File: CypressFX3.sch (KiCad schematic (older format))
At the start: 58 parts, among them CON2 AVR-JTAG-10, IC3 CyUSB30xx-BZX, J6 GSB3211311WEU, Q1 IRLML2502, Y1 19.2MHz

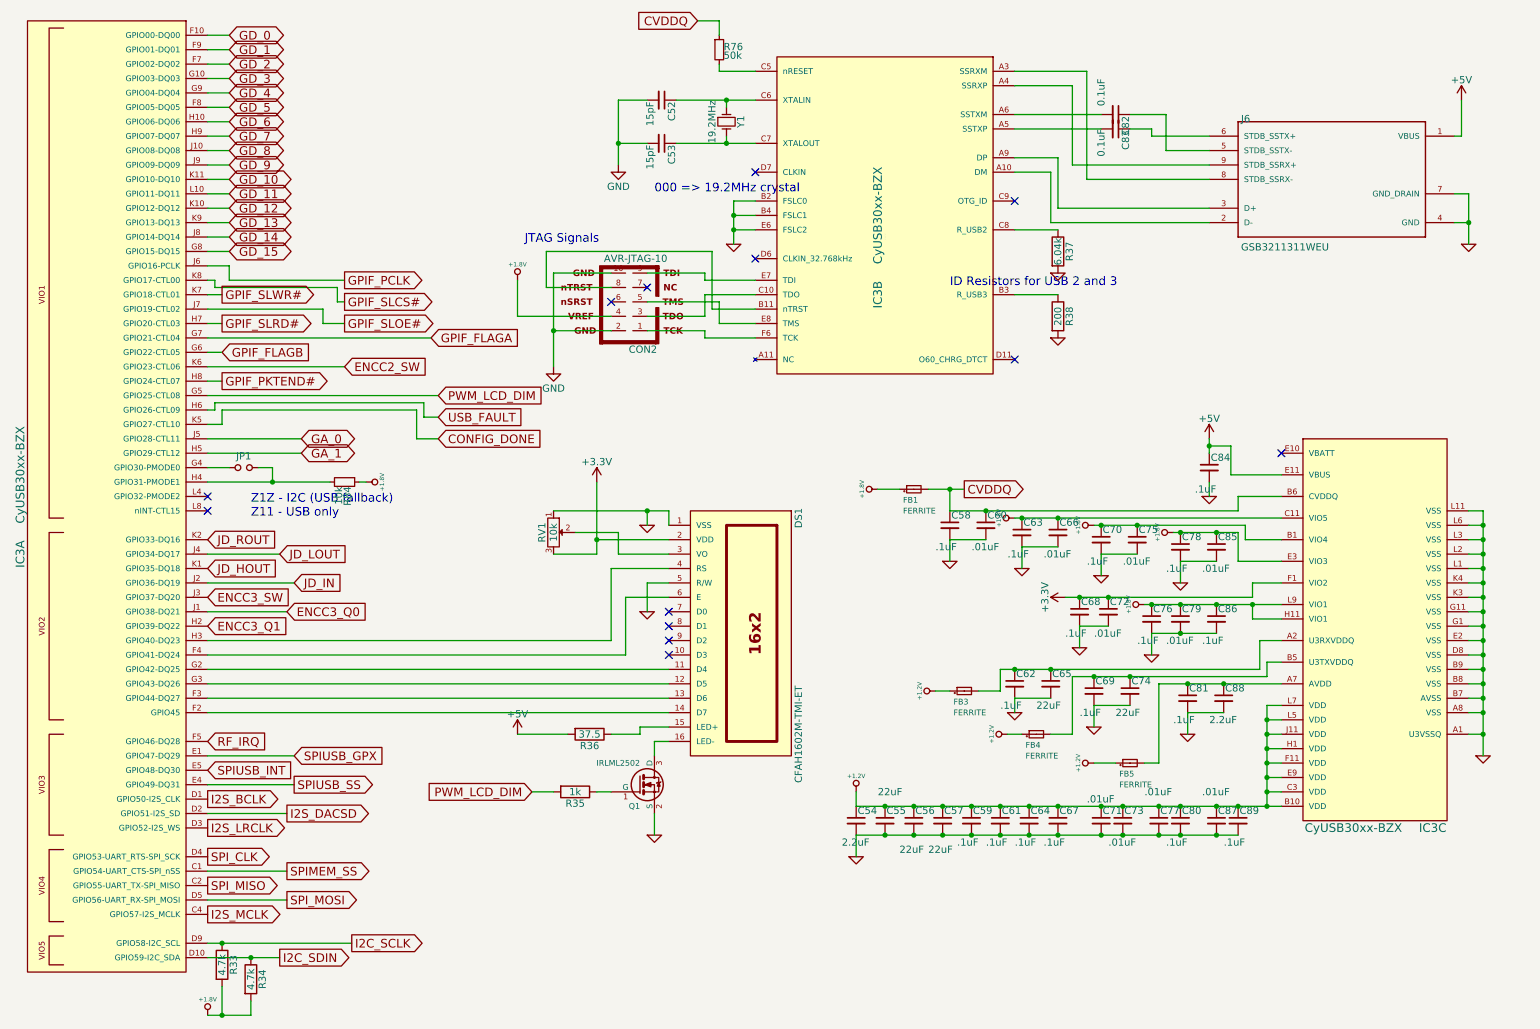
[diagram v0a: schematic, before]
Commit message: fixed all schematic/footprint errors
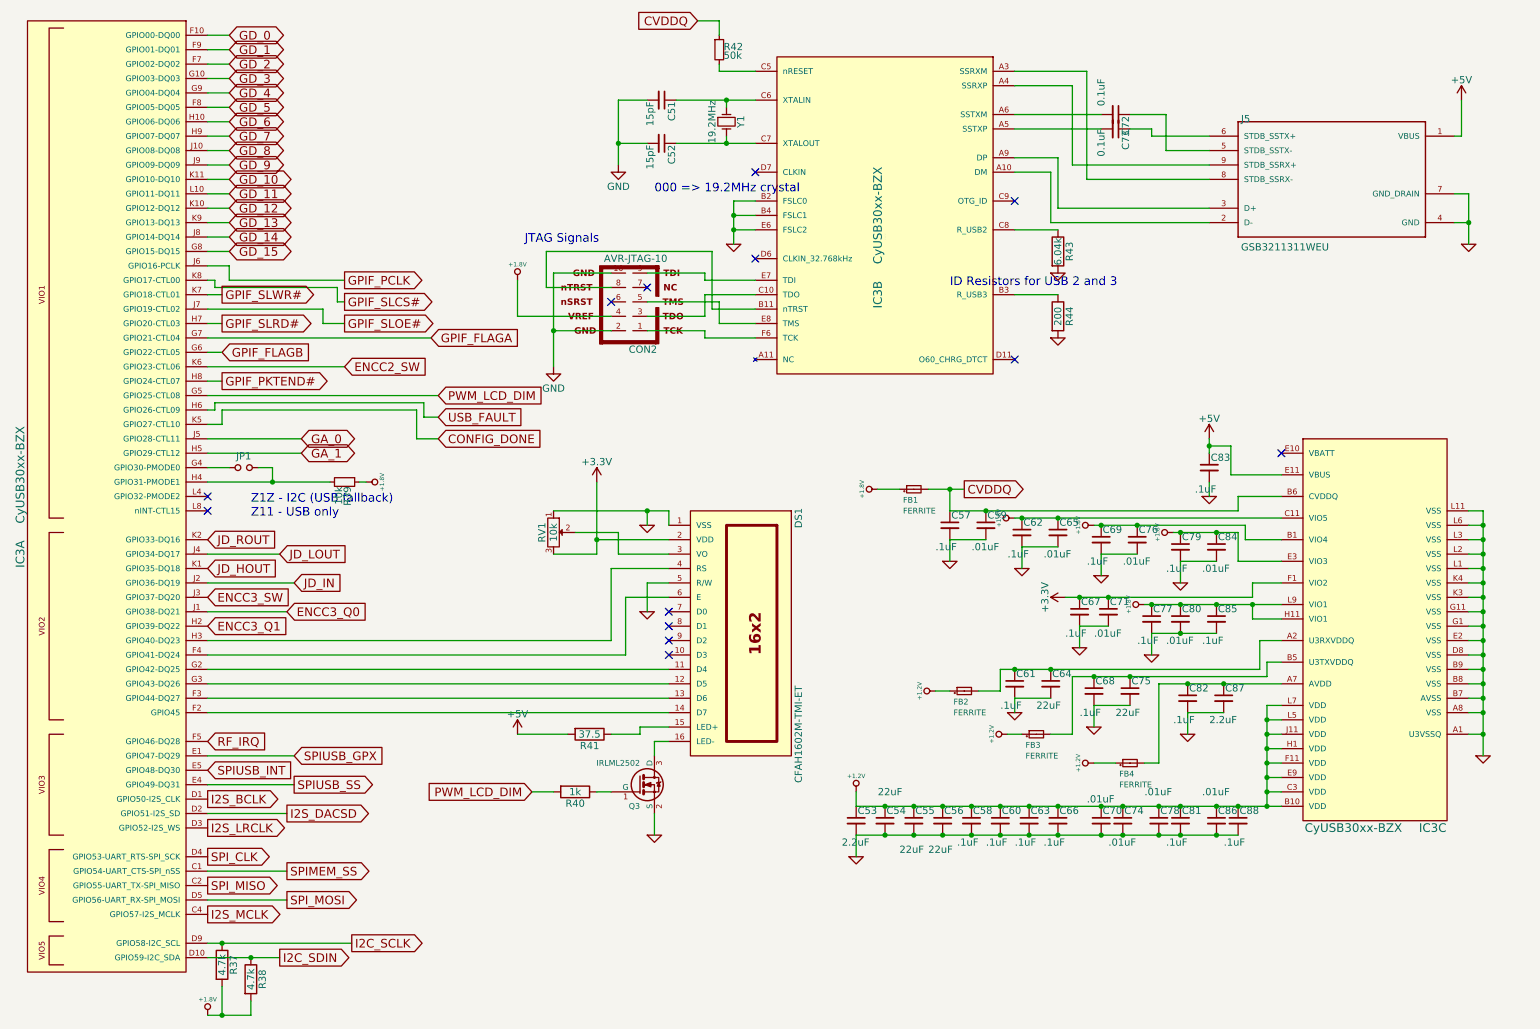
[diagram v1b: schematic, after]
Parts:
- renumbered C52 to C51, C53 to C52, C54 to C53, C55 to C54, C56 to C55, C57 to C56, C58 to C57, C59 to C58, C60 to C59, C61 to C60, C62 to C61, C63 to C62, C64 to C63, C65 to C64, C66 to C65, C67 to C66, C68 to C67, C69 to C68, C70 to C69, C71 to C70, C72 to C71, C82 to C72, C83 to C73, C73 to C74, C74 to C75, C75 to C76, C76 to C77, C77 to C78, C78 to C79, C79 to C80, C80 to C81, C81 to C82, C84 to C83, C85 to C84, C86 to C85, C87 to C86, C88 to C87, C89 to C88, FB3 to FB2, FB4 to FB3, FB5 to FB4, J6 to J5, Q1 to Q3, R33 to R37, R34 to R38, R84 to R39, R35 to R40, R36 to R41, R76 to R42, R37 to R43, R38 to R44

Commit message: started PCBnew trivial connections and BGA interface, shuffled some net connections, etc.
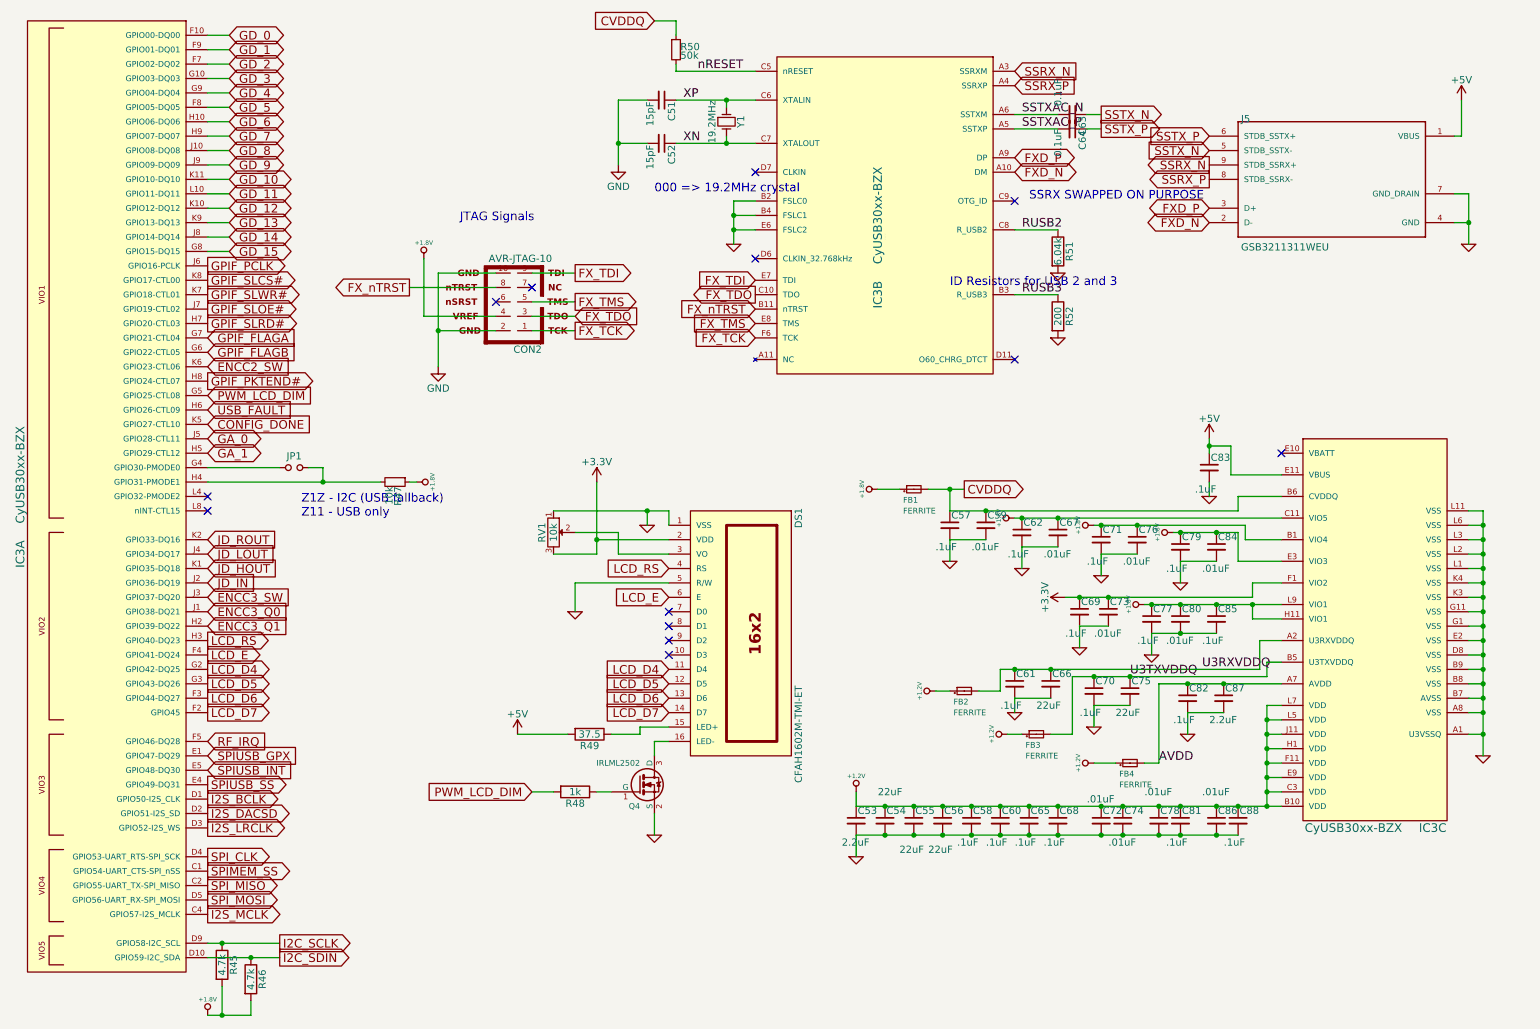
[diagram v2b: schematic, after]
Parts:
- IC3: footprint CYUSB3014-BZXCT:BGA121C80P11X11_1000X1000X110 -> DFTcustom:BGA121_08mm
- renumbered C72 to C63, C73 to C64, C63 to C65, C64 to C66, C65 to C67, C66 to C68, C67 to C69, C68 to C70, C69 to C71, C70 to C72, C71 to C73, Q3 to Q4, R37 to R45, R38 to R46, R39 to R47, R40 to R48, R41 to R49, R42 to R50, R43 to R51, R44 to R52
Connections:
- net LCD_D7: now reaches DS1.14 (D7), IC3.F2 (GPIO45)
- net LCD_D6: now reaches DS1.13 (D6), IC3.F3 (GPIO44-DQ27)
- net LCD_E: now reaches DS1.6 (E), IC3.F4 (GPIO41-DQ24)
- net LCD_D4: now reaches DS1.11 (D4), IC3.G2 (GPIO42-DQ25)
- net LCD_D5: now reaches DS1.12 (D5), IC3.G3 (GPIO43-DQ26)
- net LCD_RS: now reaches DS1.4 (RS), IC3.H3 (GPIO40-DQ23)
- net FXD_N: now reaches IC3.A10 (DM), J5.2 (D-)
- net SSRX_N: now reaches IC3.A3 (SSRXM)
- net SSRX_N: now also J5.9 (STDB_SSRX+); no longer J5.8 (STDB_SSRX-)
- net SSRX_P: now reaches IC3.A4 (SSRXP)
- net SSRX_P: now also J5.8 (STDB_SSRX-); no longer J5.9 (STDB_SSRX+)
- net SSTXAC_P: now reaches C64.2, IC3.A5 (SSTXP)
- net SSTXAC_N: now reaches C63.2, IC3.A6 (SSTXM)
- net FXD_P: now reaches IC3.A9 (DP), J5.3 (D+)
- net FX_nTRST: now reaches CON2.8, IC3.B11 (nTRST)
- net RUSB3: now reaches IC3.B3 (R_USB3), R52.1
- net FX_TDO: now reaches CON2.3, IC3.C10 (TDO)
- net nRESET: now reaches IC3.C5 (nRESET), R50.2
- net XP: now reaches C51.1, IC3.C6 (XTALIN), Y1.1
- net XN: now reaches C52.1, IC3.C7 (XTALOUT), Y1.2
- net RUSB2: now reaches IC3.C8 (R_USB2), R51.1
- net FX_TDI: now reaches CON2.9, IC3.E7 (TDI)
- net FX_TMS: now reaches CON2.5, IC3.E8 (TMS)
- net FX_TCK: now reaches CON2.1, IC3.F6 (TCK)
- net U3RXVDDQ: now reaches C61.1, C66.1, FB2.2, IC3.A2 (U3RXVDDQ)
- net AVDD: now reaches C82.1, C87.1, FB4.2, IC3.A7 (AVDD)
- net U3TXVDDQ: now reaches C70.1, C75.1, FB3.2, IC3.B5 (U3TXVDDQ)
- net SSTX_N: now reaches C63.1, J5.5 (STDB_SSTX-)
- net SSTX_P: now reaches C64.1, J5.6 (STDB_SSTX+)
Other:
- note added: "SSRX SWAPPED ON PURPOSE"
- moved on the sheet: C63, C64, CON2, JP1, R47, R50

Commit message: jan17review
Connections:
- net FX_P0: now reaches IC3.G4 (GPIO30-PMODE0), JP1.1
- net FX_P1: now reaches IC3.H4 (GPIO31-PMODE1), JP1.2, R47.2
- net LCD_LED_P: now reaches DS1.15 (LED+), R49.1
- net LCD_V0: now reaches DS1.3 (VO), RV1.2
- net LCD_LED_PWM: now reaches Q4.1 (G), R48.1
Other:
- moved on the sheet: R48, R49

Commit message: annotate from scratch
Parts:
- renumbered C65 to C63, C66 to C64, C67 to C65, C68 to C66, C63 to C67, C64 to C68, R45 to R44, R46 to R45, R47 to R46, R49 to R47, R50 to R49, R51 to R50, R52 to R51

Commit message: ran all FX3 BGA traces
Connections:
- net GND: no longer J5.4 (GND), J5.7 (GND_DRAIN)
- new net GNDPWR: J5.4 (GND), J5.7 (GND_DRAIN)

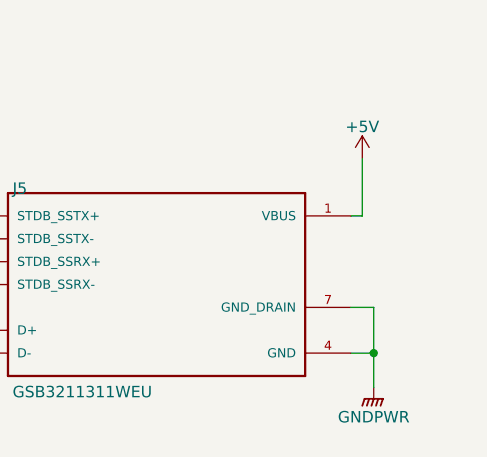
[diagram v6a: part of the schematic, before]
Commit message: added power jack detection and logic
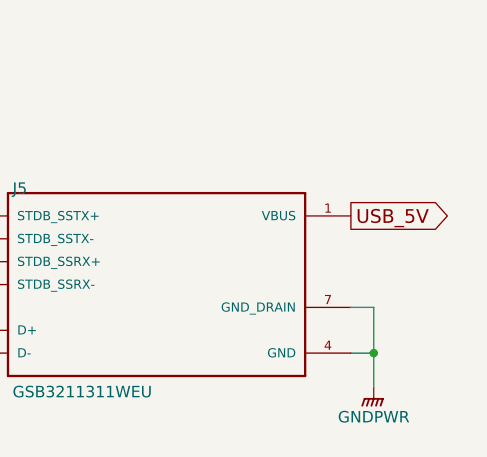
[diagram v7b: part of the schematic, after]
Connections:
- net +5V: no longer J5.1 (VBUS)
- new net USB_5V: J5.1 (VBUS)

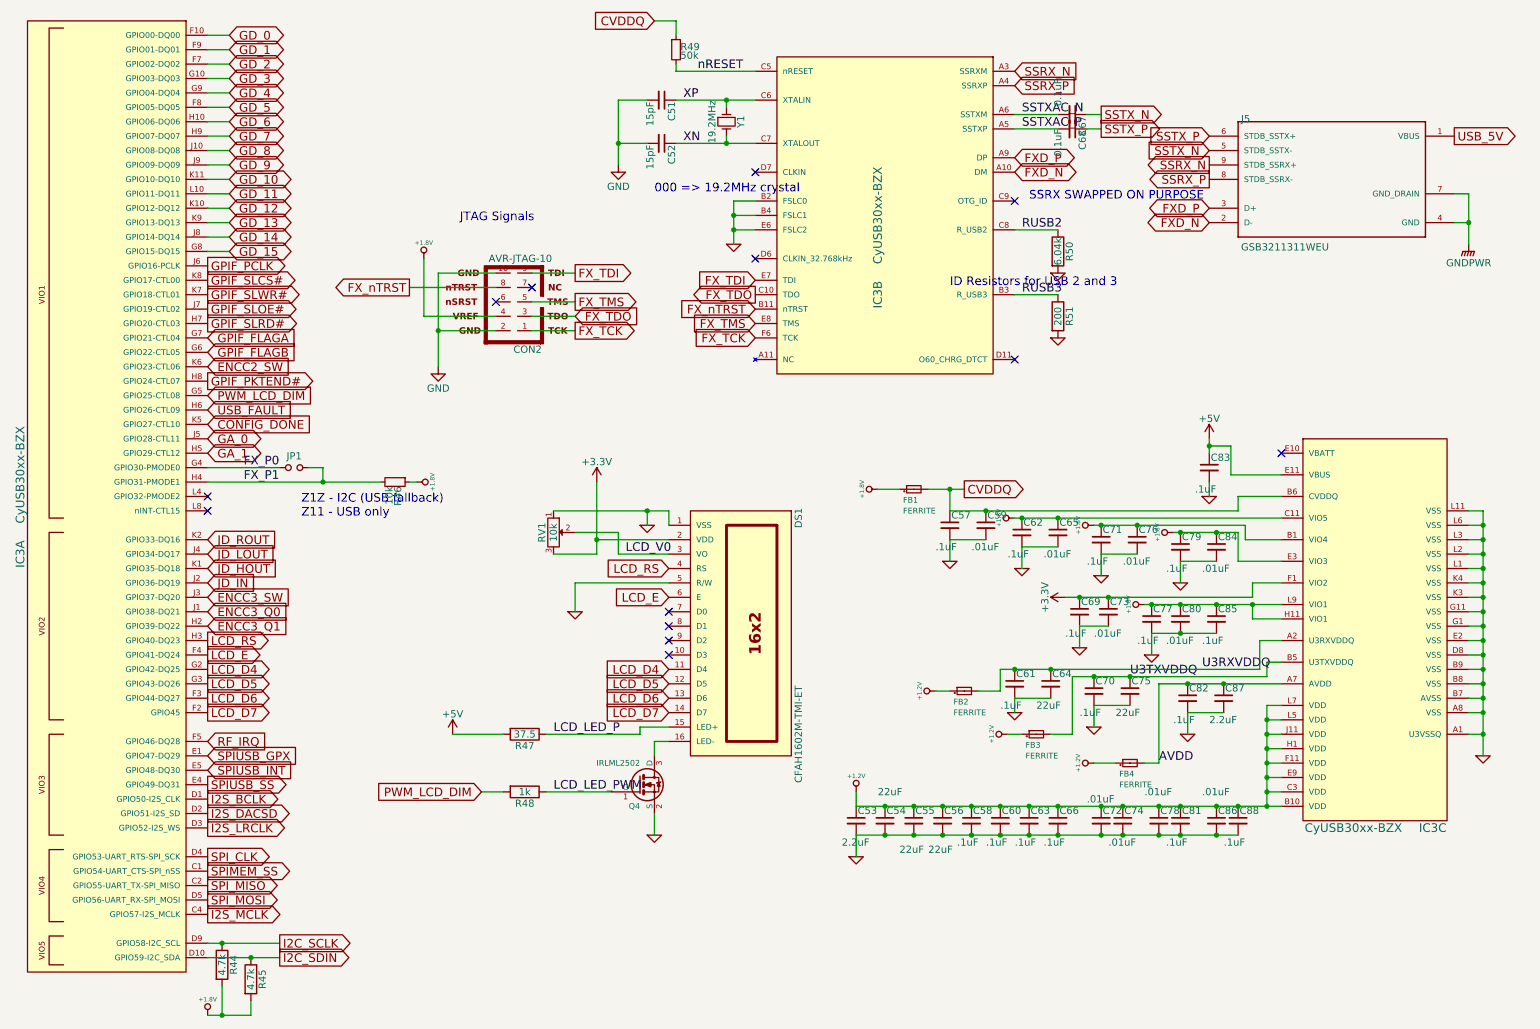
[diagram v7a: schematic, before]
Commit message: reannotated, created some footprints
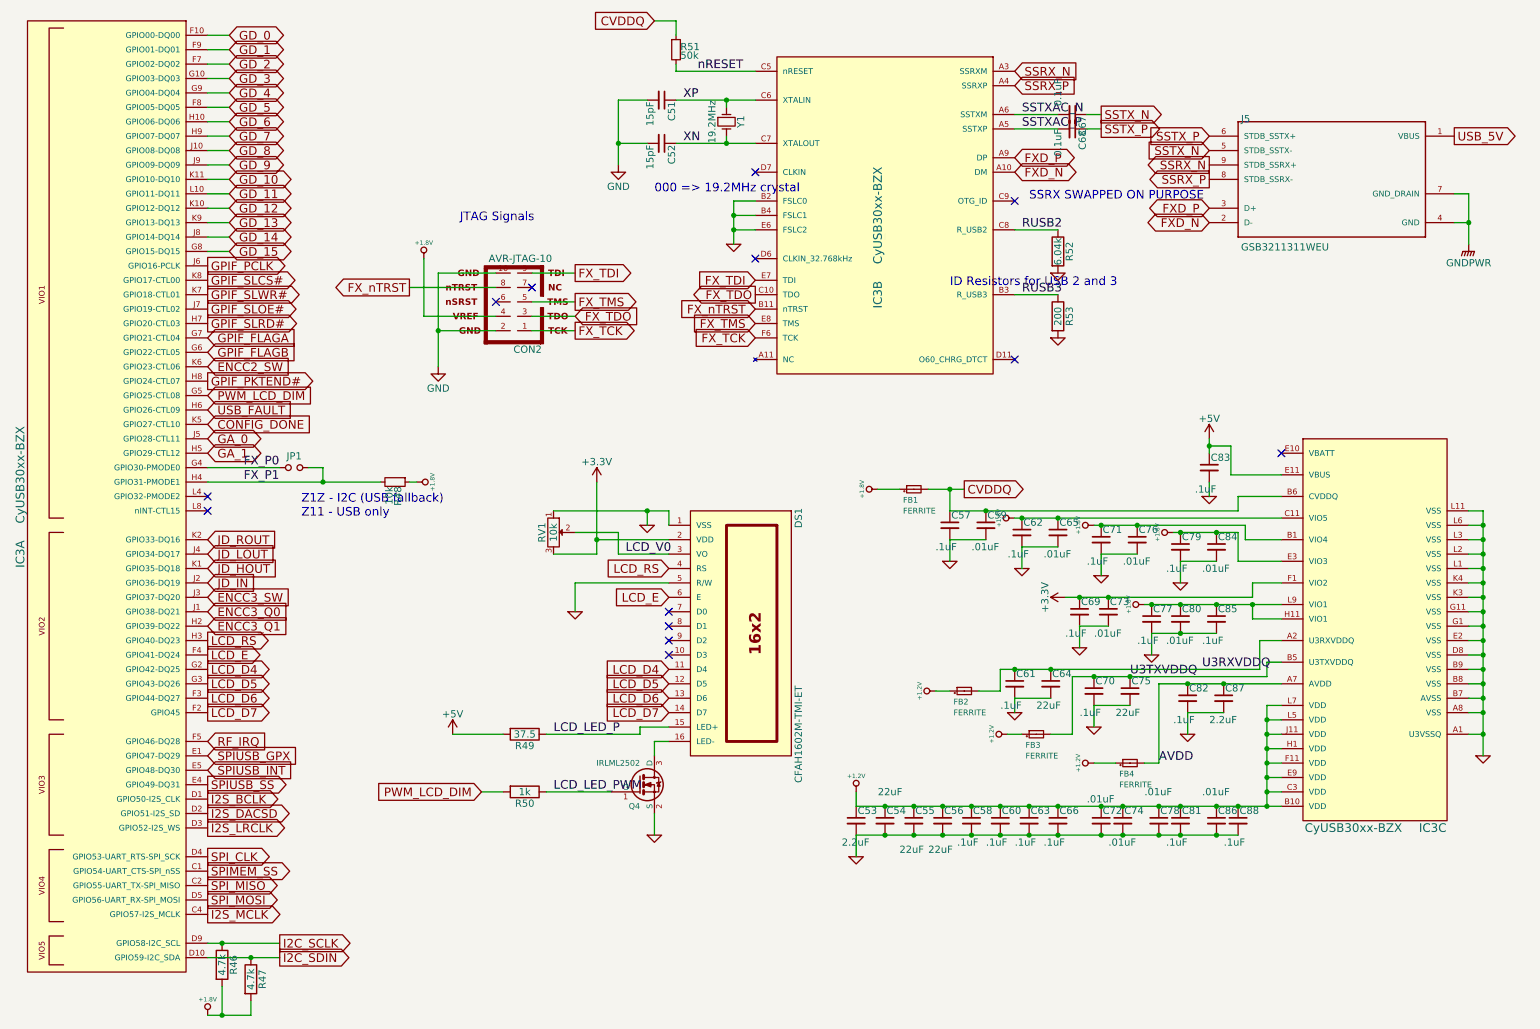
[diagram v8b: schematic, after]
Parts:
- renumbered R44 to R46, R45 to R47, R46 to R48, R47 to R49, R48 to R50, R49 to R51, R50 to R52, R51 to R53
